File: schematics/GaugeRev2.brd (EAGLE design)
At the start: 81 x 81 mm, 37 parts, among them U1 ARDUINO_MINI, U2 VID29, U3 FT232RL-BASICSSOP

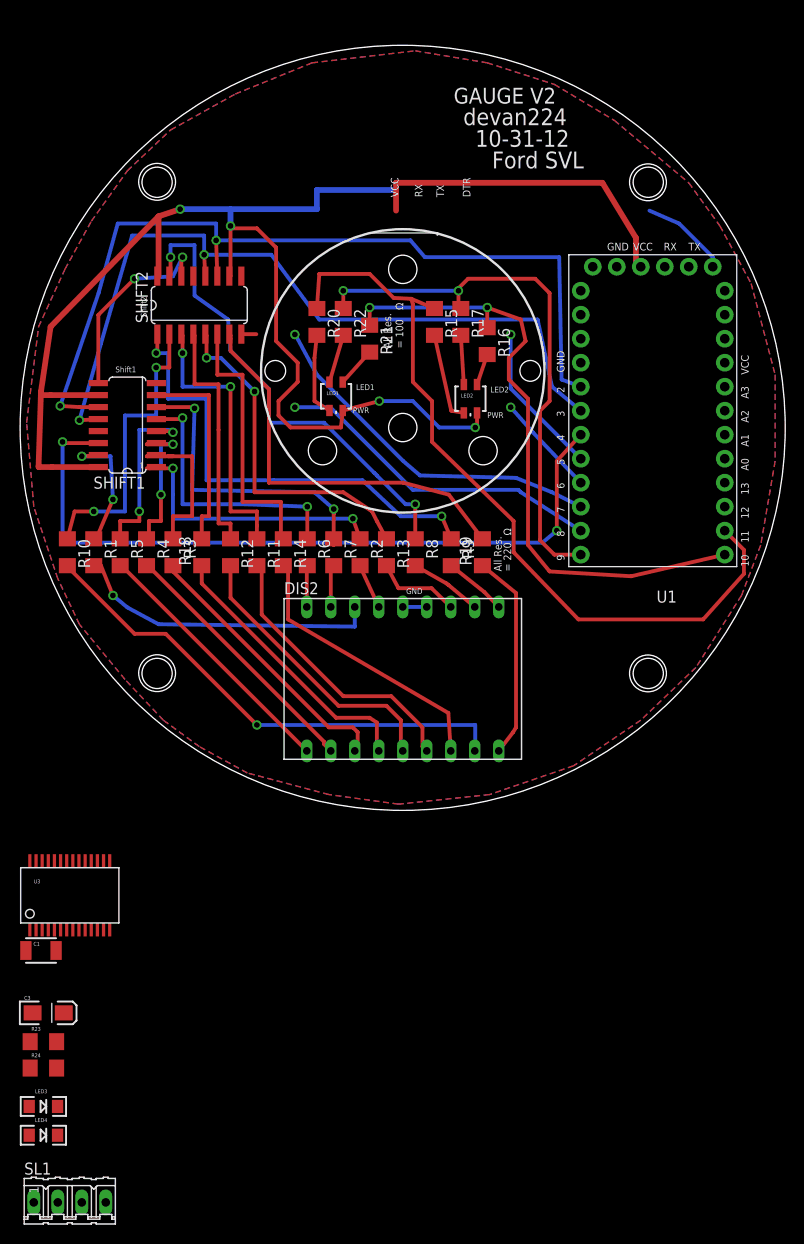
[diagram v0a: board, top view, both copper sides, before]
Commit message: layout completed for V3
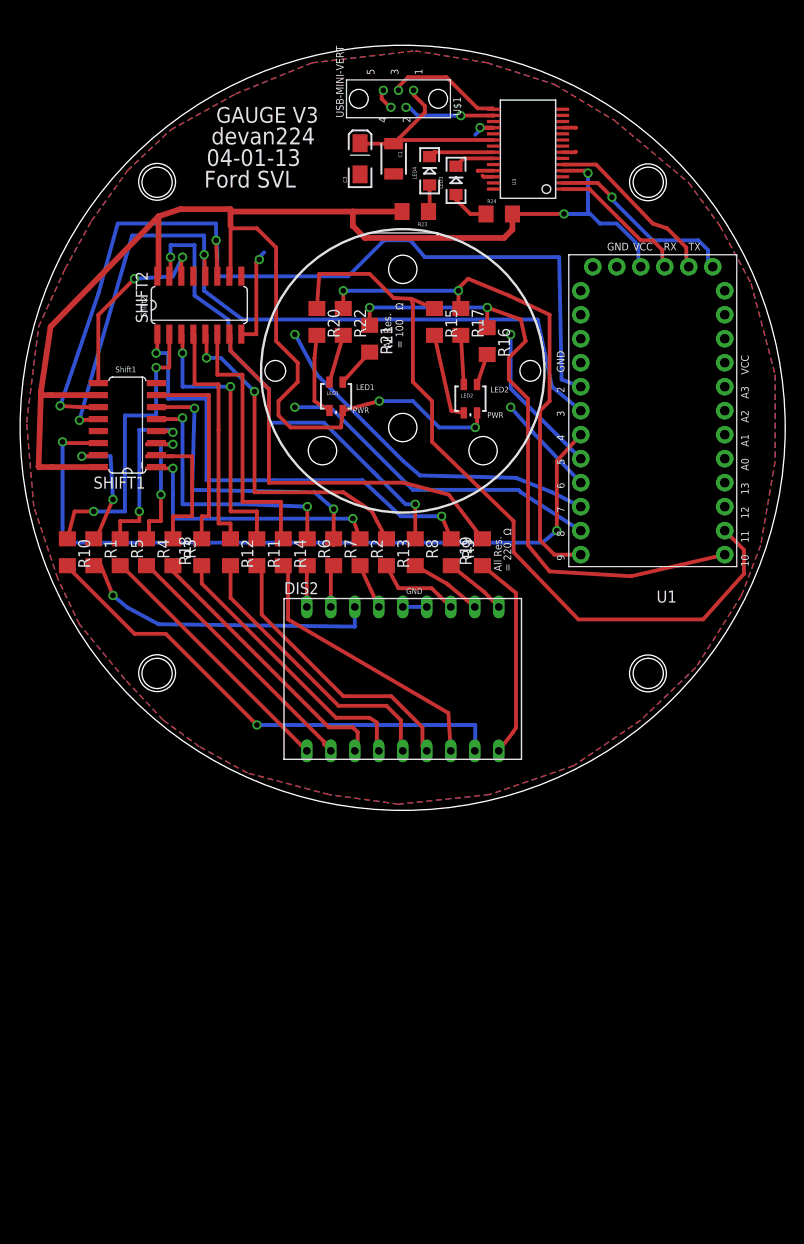
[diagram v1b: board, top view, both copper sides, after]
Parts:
- removed SL1: (no value), con-amp-quick:04P
- added U$1: USB-MINI-VERT, Evans:USB-MINI-VERT
- moved LED4 110.0 mm to (43.9, 68.6), turned to 90 degrees
- moved LED3 107.3 mm to (46.7, 67.6), turned to 90 degrees
- moved R24 102.5 mm to (51.3, 64.0)
- moved R23 96.3 mm to (42.4, 64.3), turned to 180 degrees
- moved C3 96.3 mm to (36.6, 69.8), turned to 90 degrees
- moved U3 92.7 mm to (54.4, 70.9), turned to 90 degrees
- moved C1 91.8 mm to (40.1, 69.8), turned to 270 degrees
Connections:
- net D+: now also U$1.D+; no longer SL1.1
- net D-: now also U$1.D-; no longer SL1.2
- net GND: now also U$1.GND, U$1.ID; no longer SL1.4
- net VBUS: now also U$1.VBUS; no longer SL1.3
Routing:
- net VBUS: track 0.00 -> 21.1 mm
- net GND: track 4.13 -> 25.1 mm, vias 0 -> 2
- net TXO: track 0.00 -> 18.8 mm
- net RXI: track 0.00 -> 15.1 mm
- net D+: track 0.00 -> 12.3 mm
- net DTR: track 9.48 -> 20.5 mm, vias 0 -> 1
- net D-: track 0.00 -> 9.63 mm, vias 0 -> 1
- net VCC: track 170.7 -> 180.3 mm
- net N$18: track 0.00 -> 6.95 mm
- net CLOCK: track 92.5 -> 97.8 mm
- net N$28: track 0.00 -> 4.34 mm
- net N$17: track 0.00 -> 4.31 mm
- net N$27: track 0.00 -> 2.87 mm
- net LED_R: track 58.8 -> 56.7 mm
- net LATCH: track 84.3 -> 85.6 mm
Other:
- board text added: "04-01-13"
- board text added: "GAUGE V3"
- board text removed: "10-31-12"
- board text removed: "DTR"
- board text removed: "GAUGE V2"
- board text removed: "RX"
- board text removed: "TX"
- board text removed: "VCC"
